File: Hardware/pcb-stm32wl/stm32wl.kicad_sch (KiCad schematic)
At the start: 20 parts, among them U5 STM32WL55CCU6, X1 32MHz, Y1 32.768KHz

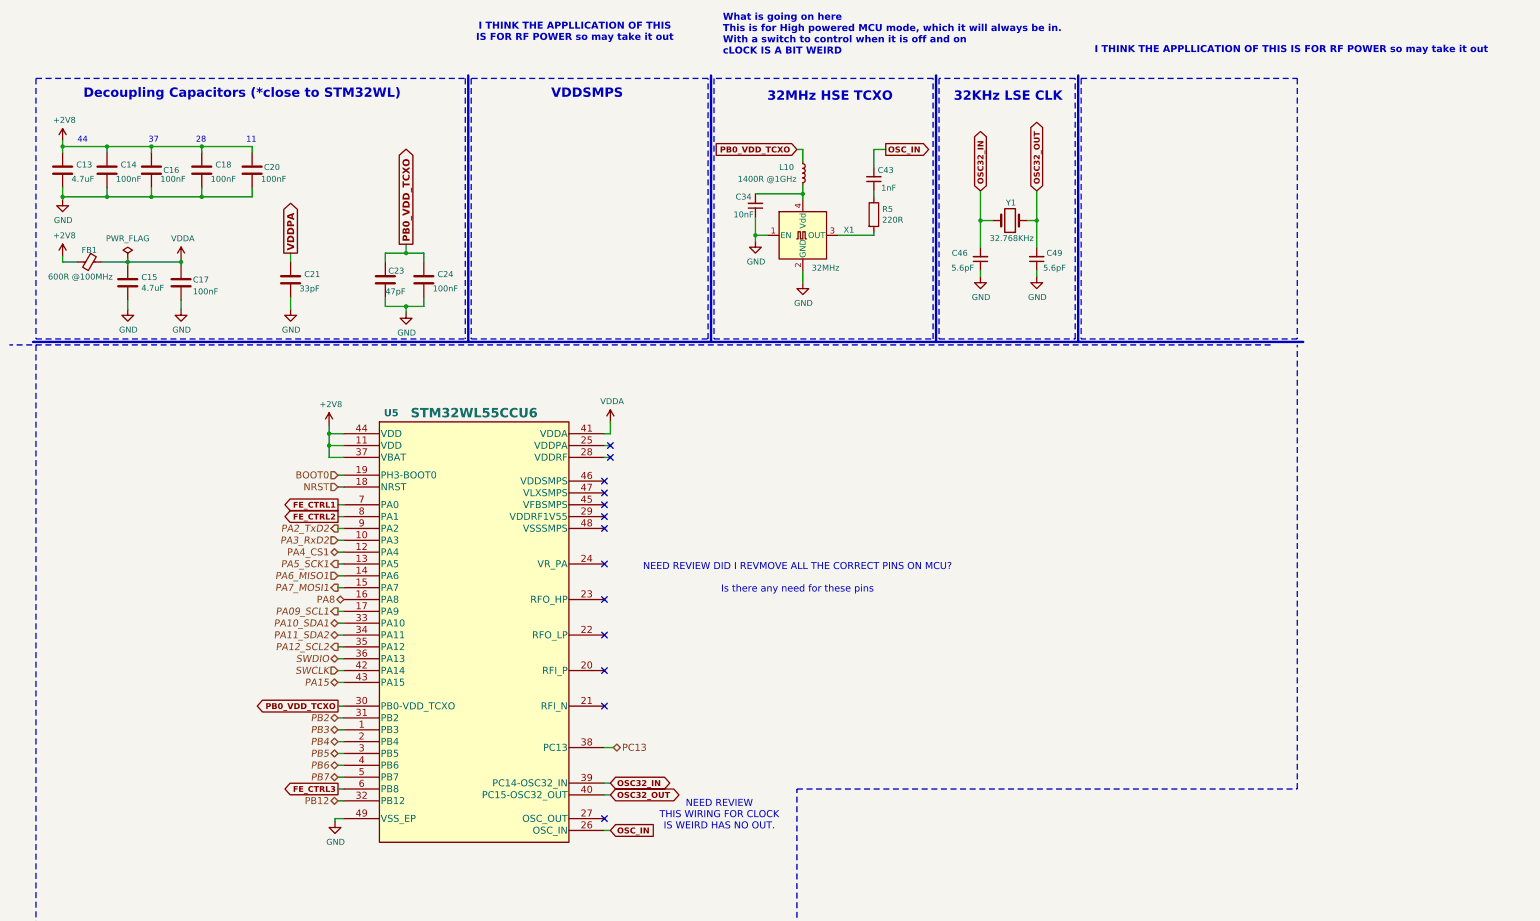
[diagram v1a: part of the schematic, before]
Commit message: rewried circuit to account ofr small details
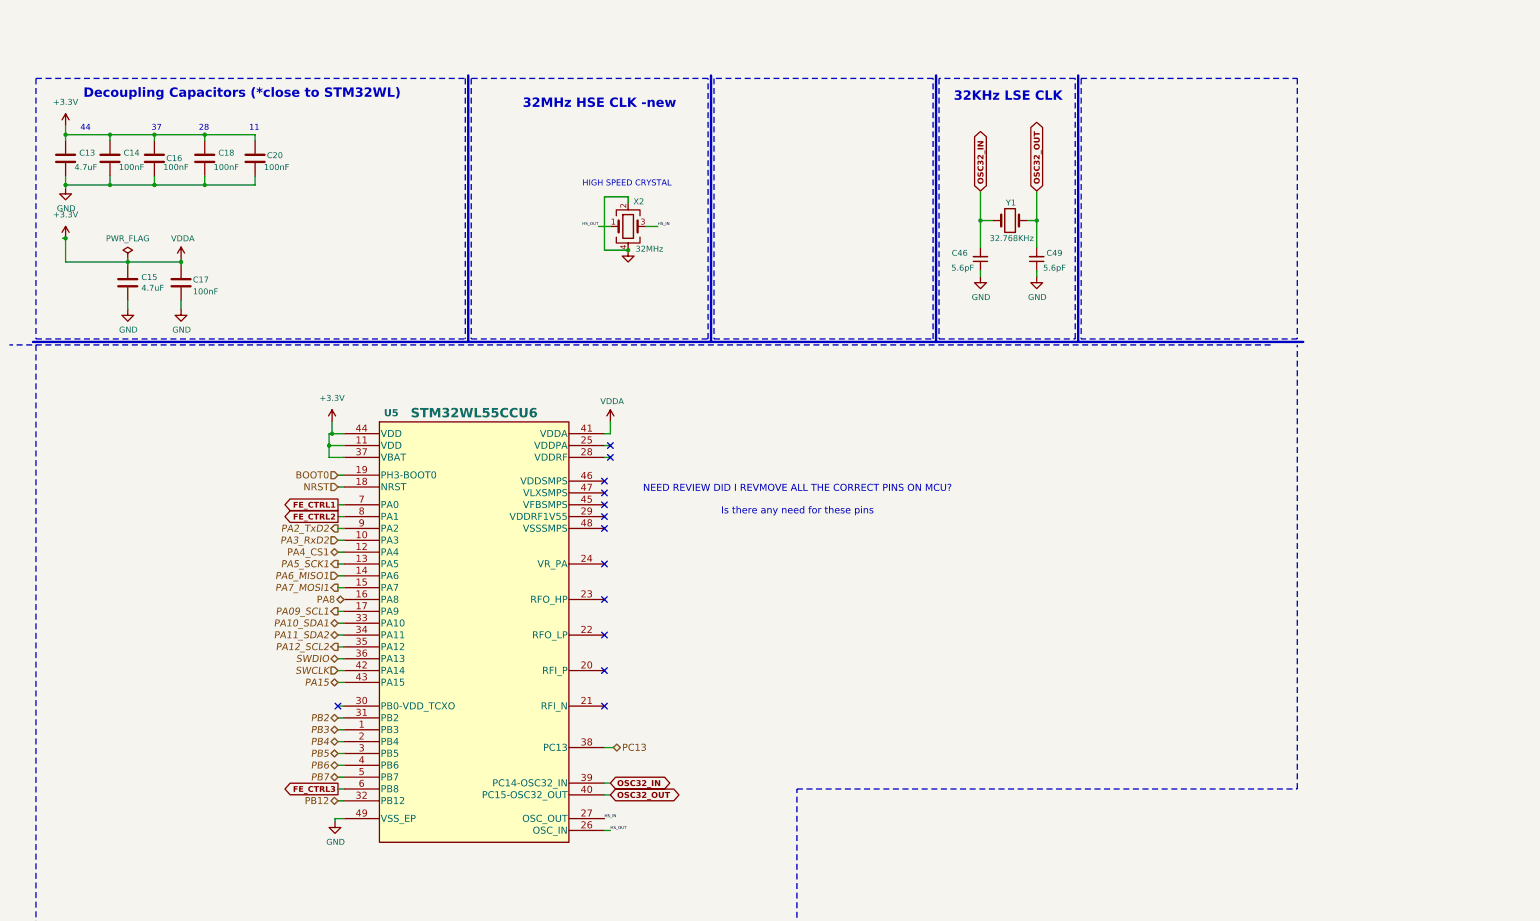
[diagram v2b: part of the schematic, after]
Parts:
- removed C21: 33pF, Capacitor_SMD:C_0402_1005Metric, symbol Device:C
- removed C23: 47pF, Capacitor_SMD:C_0402_1005Metric, symbol Device:C
- removed C24: 100nF, Capacitor_SMD:C_0402_1005Metric, symbol Device:C
- removed C34: 10nF, Capacitor_SMD:C_0402_1005Metric, symbol Device:C_Small
- removed C43: 1nF, Capacitor_SMD:C_0402_1005Metric, symbol Device:C_Small
- removed FB1: 600R @100MHz, Inductor_SMD:L_0603_1608Metric, symbol Device:Ferrite_Bead_Small
- removed L10: 1400R @1GHz, Inductor_SMD:L_0402_1005Metric, symbol Device:L_Small
- removed R5: 220R, Inductor_SMD:L_0402_1005Metric, symbol Device:R
- removed X1: 32MHz, Crystal:Crystal_SMD_Abracon_ABM10-4Pin_2.5x2.0mm, symbol node-lib-v1:TCXO-xxxMHz
- added X2: 32MHz, NX2016SA-32M-EXS00A-CS06465:NX2016SA32MEXS00ACS06465, symbol Device:Crystal_GND24
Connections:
- net VDDA is gone; now on net +3.3V: C15.1, C17.1, U5.41 (VDDA)
- net GND: now also X2.2, X2.4
- net HS_IN: now reaches U5.27 (OSC_OUT)
- net HS_IN: now also X2.3
- net +2V8 renamed +3.3V
- net OSC_IN renamed HS_OUT
- net HS_OUT: now also X2.1
- net PB0_VDD_TCXO: no longer names the net of U5.30 (PB0-VDD_TCXO)
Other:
- note added: "32MHz HSE CLK -new"
- note added: "HIGH SPEED CRYSTAL"
- note removed: "32MHz HSE TCXO"
- note removed: "I THINK THE APPLLICATION OF THIS IS FOR RF POWER so may take it out"
- note removed: "NEED REVIEW THIS WIRING FOR CLOCK IS WEIRD HAS NO OUT."
- note removed: "VDDSMPS"
- note removed: "What is going on here This is for High powered MCU mode, which it will always be in. With a switch to control when it is off and on cLOCK IS A BIT WEIRD"
- moved on the sheet: C13, C14, C16, C18, C20

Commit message: review session 2
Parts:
- added U1: NUCLEO-L476RG, NUCLEO-L476RG:MODULE_NUCLEO-L476RG, symbol NUCLEO-L476RG:NUCLEO-L476RG

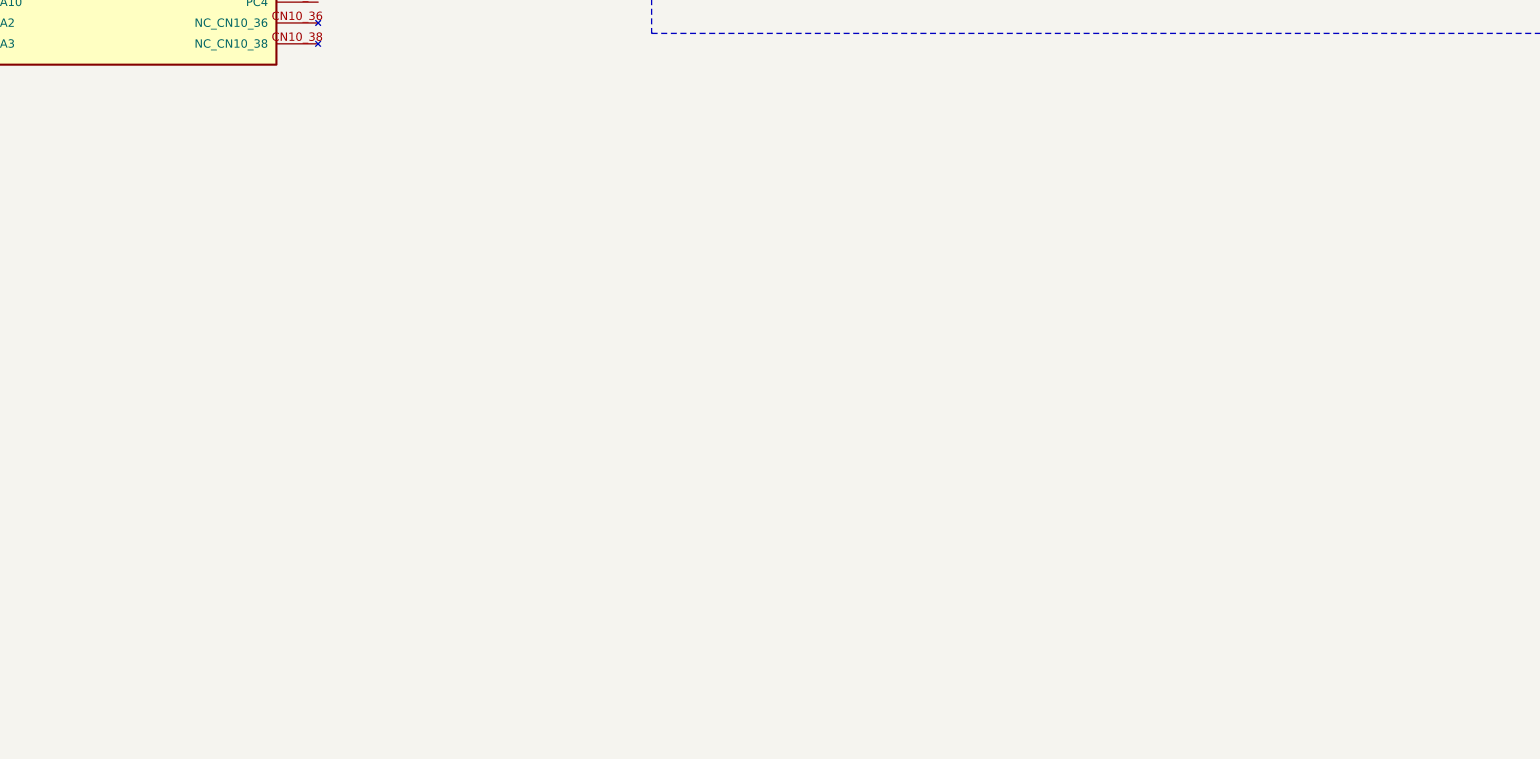
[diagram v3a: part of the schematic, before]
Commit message: added USB-C for possibility of usage
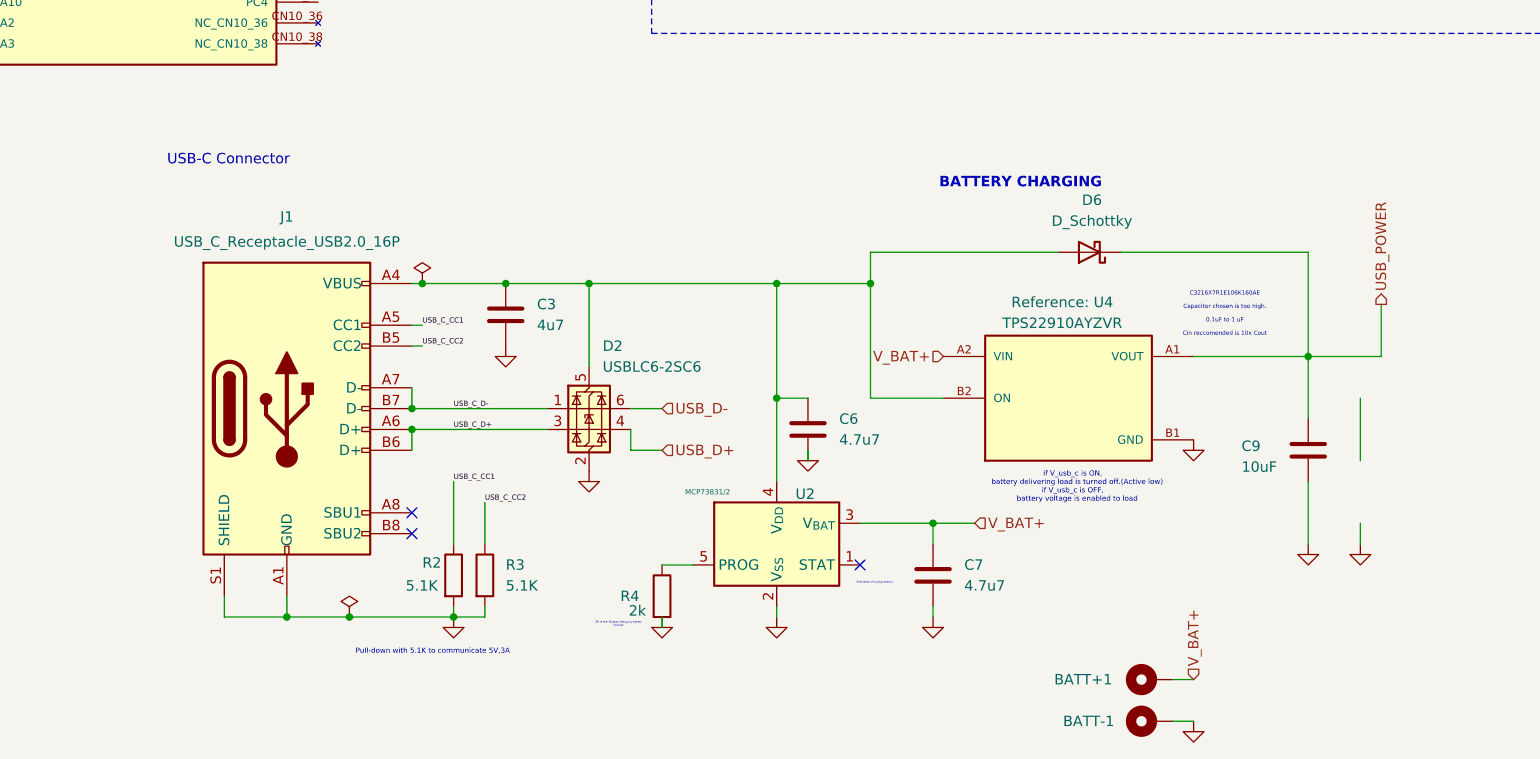
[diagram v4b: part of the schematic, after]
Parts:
- added BATT+1, BATT-1: MountingHole_Pad, MountingHole:MountingHole_2.2mm_M2_Pad, symbol Mechanical:MountingHole_Pad
- added C3: 4u7, Capacitor_SMD:C_0603_1608Metric, symbol Device:C
- added C6, C7: 4.7u7, Capacitor_SMD:C_0603_1608Metric, symbol Device:C
- added C9: 10uF, Capacitor_SMD:C_1206_3216Metric, symbol Device:C
- added D2: USBLC6-2SC6, Package_TO_SOT_SMD:SOT-23-6, symbol Power_Protection:USBLC6-2SC6
- added D6: D_Schottky, Diode_SMD:D_SOD-323F, symbol Device:D_Schottky
- added J1: USB_C_Receptacle_USB2.0_16P, Connector_USB:USB_C_Receptacle_GCT_USB4105-xx-A_16P_TopMnt_Horizontal, symbol Connector:USB_C_Receptacle_USB2.0_16P
- added R2, R3: 5.1K, Resistor_SMD:R_0603_1608Metric, symbol Device:R
- added R4: 2k, Resistor_SMD:R_0603_1608Metric, symbol Device:R
- added U2: MCP73831/2, Package_TO_SOT_SMD:SOT-23-5, symbol Battery_Management:MCP73831-2-OT
- added U4: TPS22910AYZVR, TPS22910A:BGA4N50P2X2_88X88X50N, symbol TPS22910AYZVR:TPS22910AYZVR
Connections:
- net GND: now also BATT-1.1, C3.2, C6.2, C7.2, C9.2, D2.2 (GND), J1.A1 (GND), J1.A12 (GND), J1.B1 (GND), J1.B12 (GND), J1.S1 (SHIELD), R2.2, R3.2, R4.2, U2.2 (V_{SS}), U4.B1 (GND)
- new net: C3.1, C6.1, D2.5 (VBUS), D6.2 (A), J1.A4 (VBUS), J1.A9 (VBUS), J1.B4 (VBUS), J1.B9 (VBUS), U2.4 (V_{DD}), U4.B2 (ON)
- new net: R4.1, U2.5 (PROG)
- new net USB_C_CC1: J1.A5 (CC1), R2.1
- new net USB_C_CC2: J1.B5 (CC2), R3.1
- new net USB_C_D+: D2.3 (I/O2), J1.A6 (D+), J1.B6 (D+)
- new net USB_C_D-: D2.1 (I/O1), J1.A7 (D-), J1.B7 (D-)
- new net USB_D+: D2.4 (I/O2)
- new net USB_D-: D2.6 (I/O1)
- new net USB_POWER: C9.1, D6.1 (K), U4.A1 (VOUT)
- new net V_BAT+: BATT+1.1, C7.1, U2.3 (V_{BAT}), U4.A2 (VIN)
- no-connect marks 13 -> 16
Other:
- note added: "2K is the fastest charging speed 500mA"
- note added: "BATTERY CHARGING"
- note added: "C3216X7R1E106K160AE Capacitor chosen is too high. 0.1uF to 1 uF Cin reccomended is 10x Cout"
- note added: "Indicates charging status"
- note added: "Pull-down with 5.1K to communicate 5V,3A"
- note added: "USB-C Connector"
- note added: "if V_usb_c is ON, battery delivering load is turned off.(Active low) if V_usb_c is OFF, battery voltage is enabled to load"
